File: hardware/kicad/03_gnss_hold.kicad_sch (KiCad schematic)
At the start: 0 parts

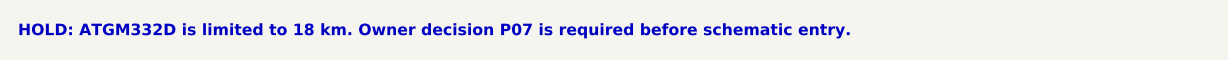
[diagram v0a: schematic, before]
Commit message: docs: accept GNSS and removable 2S direction
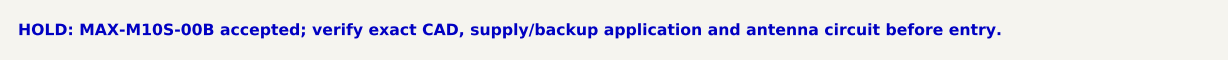
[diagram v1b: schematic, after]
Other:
- note added: "HOLD: MAX-M10S-00B accepted; verify exact CAD, supply/backup application and antenna circuit before entry."
- note removed: "HOLD: ATGM332D is limited to 18 km. Owner decision P07 is required before schematic entry."
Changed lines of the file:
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@@
 	(paper "A4")
 	(title_block (title "03 GNSS - HOLD") (rev "architecture-gate"))
-	(text "HOLD: ATGM332D is limited to 18 km. Owner decision P07 is required before schematic entry." (exclude_from_sim no) (at 25.4 30.48 0) (effects (font (size 1.27 1.27) (bold yes)) (justify left bottom)))
+	(text "HOLD: MAX-M10S-00B accepted; verify exact CAD, supply/backup application and antenna circuit before entry." (exclude_from_sim no) (at 25.4 30.48 0) (effects (font (size 1.27 1.27) (bold yes)) (justify left bottom)))
 	(sheet_instances (path "/" (page "1")))
 	(embedded_fonts no)
